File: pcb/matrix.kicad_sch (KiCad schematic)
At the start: 69 parts, among them J1 Conn_01x02, J2 USB_C_Receptacle_USB2.0_14P, SW1 SW_Push, SW2 SW_Push, SW3 SW_Push, SW4 SW_Push, U1 ESP32-S3-MINI-1U, U2 AP2112K-3.3

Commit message: Update silkscreen
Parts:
- renumbered TP9 to 3V3, TP8 to BAT1, TP1 to CP1, TP2 to CP2, TP3 to CP3, TP4 to CP4, TP5 to CP5, TP6 to CP6, TP7 to GND1, TP10 to USB1
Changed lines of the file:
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@@
 		(dnp no)
 		(fields_autoplaced yes)
-		(property "Reference" "TP1"
+		(property "Reference" "CP1"
 			(at 200.66 94.7419 0)
 			(effects
@@
 			(project ""
 				(path "/dedde073-c051-4814-9913-31ee2067ce3b"
-					(reference "TP1")
+					(reference "CP1")
 					(unit 1)
 				)
@@
 		(dnp no)
 		(fields_autoplaced yes)
-		(property "Reference" "TP10"
+		(property "Reference" "USB1"
 			(at 82.55 47.4979 0)
 			(effects
@@
 			(project ""
 				(path "/dedde073-c051-4814-9913-31ee2067ce3b"
-					(reference "TP10")
+					(reference "USB1")
 					(unit 1)
 				)
@@
 		(dnp no)
 		(fields_autoplaced yes)
-		(property "Reference" "TP6"
+		(property "Reference" "CP6"
 			(at 200.66 132.8419 0)
 			(effects
@@
 			(project "simple"
 				(path "/dedde073-c051-4814-9913-31ee2067ce3b"
-					(reference "TP6")
+					(reference "CP6")
 					(unit 1)
 				)
@@
 		(dnp no)
 		(fields_autoplaced yes)
-		(property "Reference" "TP7"
+		(property "Reference" "GND1"
 			(at 62.23 134.1119 0)
 			(effects
@@
 			(project ""
 				(path "/dedde073-c051-4814-9913-31ee2067ce3b"
-					(reference "TP7")
+					(reference "GND1")
 					(unit 1)
 				)
@@
 		(dnp no)
 		(fields_autoplaced yes)
-		(property "Reference" "TP9"
+		(property "Reference" "3V3"
 			(at 99.568 82.55 90)
 			(effects
@@
 			(project ""
 				(path "/dedde073-c051-4814-9913-31ee2067ce3b"
-					(reference "TP9")
+					(reference "3V3")
 					(unit 1)
 				)
@@
 		(dnp no)
 		(fields_autoplaced yes)
-		(property "Reference" "TP3"
+		(property "Reference" "CP3"
 			(at 200.66 109.9819 0)
 			(effects
@@
 			(project "simple"
 				(path "/dedde073-c051-4814-9913-31ee2067ce3b"
-					(reference "TP3")
+					(reference "CP3")
 					(unit 1)
 				)
@@
 		(dnp no)
 		(fields_autoplaced yes)
-		(property "Reference" "TP2"
+		(property "Reference" "CP2"
 			(at 200.66 102.3619 0)
 			(effects
@@
 			(project "simple"
 				(path "/dedde073-c051-4814-9913-31ee2067ce3b"
-					(reference "TP2")
+					(reference "CP2")
 					(unit 1)
 				)
@@
 		(dnp no)
 		(fields_autoplaced yes)
-		(property "Reference" "TP8"
+		(property "Reference" "BAT1"
 			(at 62.23 117.3479 0)
 			(effects
@@
 			(project ""
 				(path "/dedde073-c051-4814-9913-31ee2067ce3b"
-					(reference "TP8")
+					(reference "BAT1")
 					(unit 1)
 				)
@@
 		(dnp no)
 		(fields_autoplaced yes)
-		(property "Reference" "TP5"
+		(property "Reference" "CP5"
 			(at 200.66 125.2219 0)
 			(effects
@@
 			(project "simple"
 				(path "/dedde073-c051-4814-9913-31ee2067ce3b"
-					(reference "TP5")
+					(reference "CP5")
 					(unit 1)
 				)
@@
 		(dnp no)
 		(fields_autoplaced yes)
-		(property "Reference" "TP4"
+		(property "Reference" "CP4"
 			(at 200.66 117.6019 0)
 			(effects
@@
 			(project "simple"
 				(path "/dedde073-c051-4814-9913-31ee2067ce3b"
-					(reference "TP4")
+					(reference "CP4")
 					(unit 1)
 				)

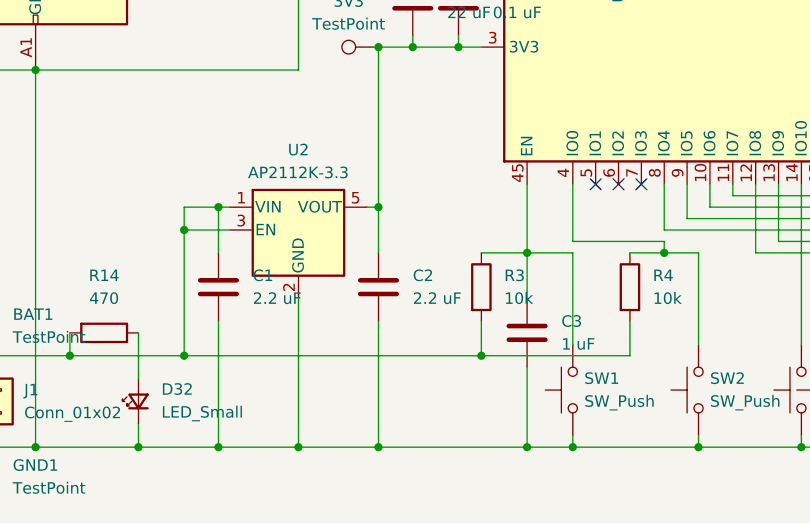
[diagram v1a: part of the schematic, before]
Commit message: Fix incorrect voltage
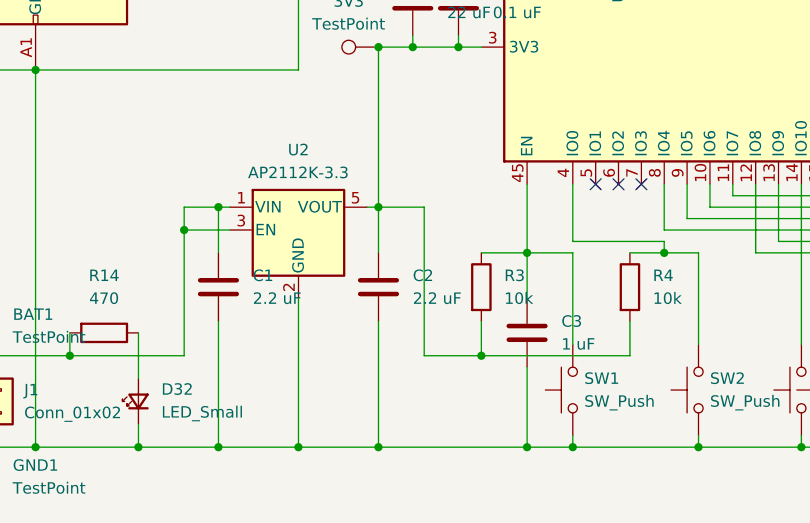
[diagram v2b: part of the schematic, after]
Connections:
- net at 3V3.1, C2.1, C4.2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: now also R3.2, R4.2
- net at BAT1.1, C1.1, J1.1 (Pin_1)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: no longer R3.2, R4.2
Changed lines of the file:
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@@
 	)
 	(junction
+		(at 114.3 121.92)
+		(diameter 0)
+		(color 0 0 0 0)
+	)
+	(junction
 		(at 55.88 125.73)
 		(diameter 0)
@@
 	)
 	(junction
-		(at 114.3 121.92)
-		(diameter 0)
-		(color 0 0 0 0)
-	)
-	(junction
 		(at 102.87 105.41)
 		(diameter 0)
@@
 	)
 	(junction
-		(at 81.28 121.92)
-		(diameter 0)
-		(color 0 0 0 0)
-	)
-	(junction
 		(at 204.47 121.92)
 		(diameter 0)
@@
 	(wire
 		(pts
-			(xy 81.28 121.92) (xy 114.3 121.92)
-		)
-		(stroke
-			(width 0)
-			(type default)
-		)
-	)
-	(wire
-		(pts
 			(xy 214.63 100.33) (xy 212.09 100.33)
 		)
@@
 	(wire
 		(pts
+			(xy 102.87 105.41) (xy 107.95 105.41)
+		)
+		(stroke
+			(width 0)
+			(type default)
+		)
+	)
+	(wire
+		(pts
 			(xy 240.03 114.3) (xy 242.57 114.3)
 		)
@@
 	(wire
 		(pts
-			(xy 130.81 118.11) (xy 130.81 121.92)
-		)
-		(stroke
-			(width 0)
-			(type default)
-		)
-	)
-	(wire
-		(pts
 			(xy 232.41 121.92) (xy 234.95 121.92)
 		)
@@
 	(wire
 		(pts
+			(xy 107.95 121.92) (xy 114.3 121.92)
+		)
+		(stroke
+			(width 0)
+			(type default)
+		)
+	)
+	(wire
+		(pts
 			(xy 214.63 107.95) (xy 214.63 106.68)
 		)
@@
 	(wire
 		(pts
-			(xy 114.3 121.92) (xy 130.81 121.92)
-		)
-		(stroke
-			(width 0)
-			(type default)
-		)
-	)
-	(wire
-		(pts
 			(xy 184.15 100.33) (xy 189.23 100.33)
 		)
@@
 	(wire
 		(pts
+			(xy 130.81 121.92) (xy 130.81 118.11)
+		)
+		(stroke
+			(width 0)
+			(type default)
+		)
+	)
+	(wire
+		(pts
 			(xy 229.87 101.6) (xy 232.41 101.6)
 		)
@@
 	(wire
 		(pts
+			(xy 114.3 121.92) (xy 130.81 121.92)
+		)
+		(stroke
+			(width 0)
+			(type default)
+		)
+	)
+	(wire
+		(pts
 			(xy 237.49 130.81) (xy 237.49 129.54)
 		)
@@
 		)
 		(stroke
+			(width 0)
+			(type default)
+		)
+	)
+	(wire
+		(pts
+			(xy 107.95 105.41) (xy 107.95 121.92)
+		)
+		(stroke

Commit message: Update parts
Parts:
- removed U2: AP2112K-3.3, Package_TO_SOT_SMD:SOT-23-5, symbol Regulator_Linear:AP2112K-3.3
- added U2: XC6206PxxxMR, Package_TO_SOT_SMD:SOT-23-3, symbol Regulator_Linear:XC6206PxxxMR
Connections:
- net GND: now also U2.1 (GND)
- net at 3V3.1, C2.1, C4.2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: now also U2.2 (VO)
- net at BAT1.1, C1.1, J1.1 (Pin_1)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: now also U2.3 (VI)
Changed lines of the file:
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@@
 	)
 	(junction
+		(at 93.98 132.08)
+		(diameter 0)
+		(color 0 0 0 0)
+	)
+	(junction
 		(at 227.33 99.06)
 		(diameter 0)
@@
 	)
 	(junction
-		(at 93.98 132.08)
-		(diameter 0)
-		(color 0 0 0 0)
-	)
-	(junction
 		(at 207.01 129.54)
 		(diameter 0)
@@
 	)
 	(junction
-		(at 81.28 107.95)
-		(diameter 0)
-		(color 0 0 0 0)
-	)
-	(junction
 		(at 207.01 93.98)
 		(diameter 0)
@@
 	(wire
 		(pts
-			(xy 93.98 115.57) (xy 93.98 132.08)
-		)
-		(stroke
-			(width 0)
-			(type default)
-		)
-	)
-	(wire
-		(pts
 			(xy 199.39 100.33) (xy 198.12 100.33)
 		)
@@
 	(wire
 		(pts
-			(xy 85.09 132.08) (xy 93.98 132.08)
+			(xy 93.98 113.03) (xy 93.98 132.08)
 		)
 		(stroke
@@
 	(wire
 		(pts
+			(xy 93.98 132.08) (xy 102.87 132.08)
+		)
+		(stroke
+			(width 0)
+			(type default)
+		)
+	)
+	(wire
+		(pts
 			(xy 111.76 63.5) (xy 179.07 63.5)
 		)
@@
 	(wire
 		(pts
-			(xy 81.28 105.41) (xy 81.28 107.95)
-		)
-		(stroke
-			(width 0)
-			(type default)
-		)
-	)
-	(wire
-		(pts
 			(xy 233.68 116.84) (xy 234.95 116.84)
 		)
@@
 	(wire
 		(pts
-			(xy 93.98 132.08) (xy 102.87 132.08)
+			(xy 85.09 132.08) (xy 93.98 132.08)
 		)
 		(stroke
@@
 	(wire
 		(pts
-			(xy 81.28 107.95) (xy 81.28 121.92)
+			(xy 81.28 105.41) (xy 81.28 121.92)
 		)
 		(stroke
@@
 	(wire
 		(pts
-			(xy 81.28 107.95) (xy 86.36 107.95)
-		)
-		(stroke
-			(width 0)
-			(type default)
-		)
-	)
-	(wire
-		(pts
 			(xy 210.82 127) (xy 210.82 124.46)
 		)
@@
 	)
 	(symbol
+		(lib_id "Regulator_Linear:XC6206PxxxMR")
+		(at 93.98 105.41 0)
+		(unit 1)
+		(exclude_from_sim no)
+		(in_bom yes)
+		(on_board yes)
+		(dnp no)
+		(fields_autoplaced yes)
+		(property "Reference" "U2"
+			(at 93.98 99.06 0)
+			(effects
+				(font
+					(size 1.27 1.27)
+				)
+			)
+		)
+		(property "Value" "XC6206PxxxMR"
+			(at 93.98 101.6 0)
+			(effects
+				(font
+					(size 1.27 1.27)
+				)
+			)
+		)
+		(property "Footprint" "Package_TO_SOT_SMD:SOT-23-3"
+			(at 93.98 99.695 0)
+			(effects
+				(font
+					(size 1.27 1.27)
+					(italic yes)
+				)
+				(hide yes)
+			)
+		)
+		(property "Datasheet" "https://www.torexsemi.com/file/xc6206/XC6206.pdf"
+			(at 93.98 105.41 0)
+			(effects
+				(font
+					(size 1.27 1.27)
+				)
+				(hide yes)
+			)
+		)
+		(property "Description" "Positive 60-250mA Low Dropout Regulator, Fixed Output, SOT-23"
+			(at 93.98 105.41 0)
+			(effects
+				(font
+					(size 1.27 1.27)
+				)
+				(hide yes)
+			)
+		)
+		(pin "3"
+		)
+		(pin "1"
+		)
+		(pin "2"
+		)
+		(instances
+			(project ""
+				(path "/dedde073-c051-4814-9913-31ee2067ce3b"
+					(reference "U2")
+					(unit 1)
+				)
+			)
+		)
+	)
+	(symbol
 		(lib_id "Device:C")
 		(at 102.87 114.3 0)
@@
 					(unit 1)
 				)
-			)
-		)
-	)
-	(symbol
-		(lib_id "Regulator_Linear:AP2112K-3.3")
-		(at 93.98 107.95 0)
-		(unit 1)
-		(exclude_from_sim no)
-		(in_bom yes)
-		(on_board yes)
-		(dnp no)
-		(fields_autoplaced yes)
-		(property "Reference" "U2"
-			(at 93.98 99.06 0)
-			(effects
-				(font
-					(size 1.27 1.27)
-				)
-			)
-		)
-		(property "Value" "AP2112K-3.3"
-			(at 93.98 101.6 0)
-			(effects
-				(font
-					(size 1.27 1.27)
-				)
-			)
-		)
-		(property "Footprint" "Package_TO_SOT_SMD:SOT-23-5"
-			(at 93.98 99.695 0)
-			(effects
-				(font
-					(size 1.27 1.27)
-				)
-				(hide yes)
-			)
-		)
-		(property "Datasheet" "https://www.diodes.com/assets/Datasheets/AP2112.pdf"
-			(at 93.98 105.41 0)
-			(effects
-				(font
-					(size 1.27 1.27)
-				)
-				(hide yes)
-			)
-		)
-		(property "Description" "600mA low dropout linear regulator, with enable pin, 3.8V-6V input voltage range, 3.3V fixed positive output, SOT-23-5"
-			(at 93.98 107.95 0)
-			(effects
-				(font
-					(size 1.27 1.27)
-				)
-				(hide yes)
-			)
-		)
-		(pin "3"
-		)
-		(pin "1"
-		)
-		(pin "4"
-		)
-		(pin "2"
-		)
-		(pin "5"
-		)
-		(instances
-			(project "simple"
-				(path "/dedde073-c051-4814-9913-31ee2067ce3b"
-					(reference "U2")
-					(unit 1)
-				)

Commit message: Replace components
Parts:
- removed SW4: SW_Push, Button_Switch_SMD:SW_SPST_PTS810, symbol Switch:SW_Push
- removed U1: ESP32-S3-MINI-1U, RF_Module:ESP32-S2-MINI-1U, symbol RF_Module:ESP32-S3-MINI-1U
- added U1: ESP32-C3-WROOM-02, RF_Module:ESP32-C3-WROOM-02, symbol RF_Module:ESP32-C3-WROOM-02
- SW1, SW2, SW3: footprint Button_Switch_SMD:SW_SPST_PTS810 -> Button_Switch_SMD:SW_SPST_TS-1088-xR020
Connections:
- net GND: now also U1.19 (GND), U1.9 (GND)
- net at 3V3.1, C2.1, C4.2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: now also U1.1 (3V3)
- net P5: now reaches R9.1
- net P5: now also U1.15 (IO3)
- net P4: now reaches R8.1
- net P4: now also U1.3 (IO4)
- net P3: now reaches R7.1
- net P3: now also U1.4 (IO5)
- net P2: now reaches R6.1
- net P2: now also U1.5 (IO6)
- net P1: now reaches R5.1
- net P1: now also U1.6 (IO7)
- net at SW3.2: now also U1.10 (IO10)
- net USB-: now reaches R11.2
- net USB-: now also U1.13 (IO18)
- net USB+: now reaches R12.2
- net USB+: now also U1.14 (IO19)
- net at R4.1, SW2.2: now also U1.18 (IO0)
- net at C3.1, R3.1, SW1.2: now also U1.2 (EN)
- net P6: now reaches R10.1
- net P6: now also U1.17 (IO1)
- no-connect marks 26 -> 5
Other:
- moved on the sheet: CP1, CP2, CP3, CP4, CP5, CP6, D1, D10, D11, D12, D13, D14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

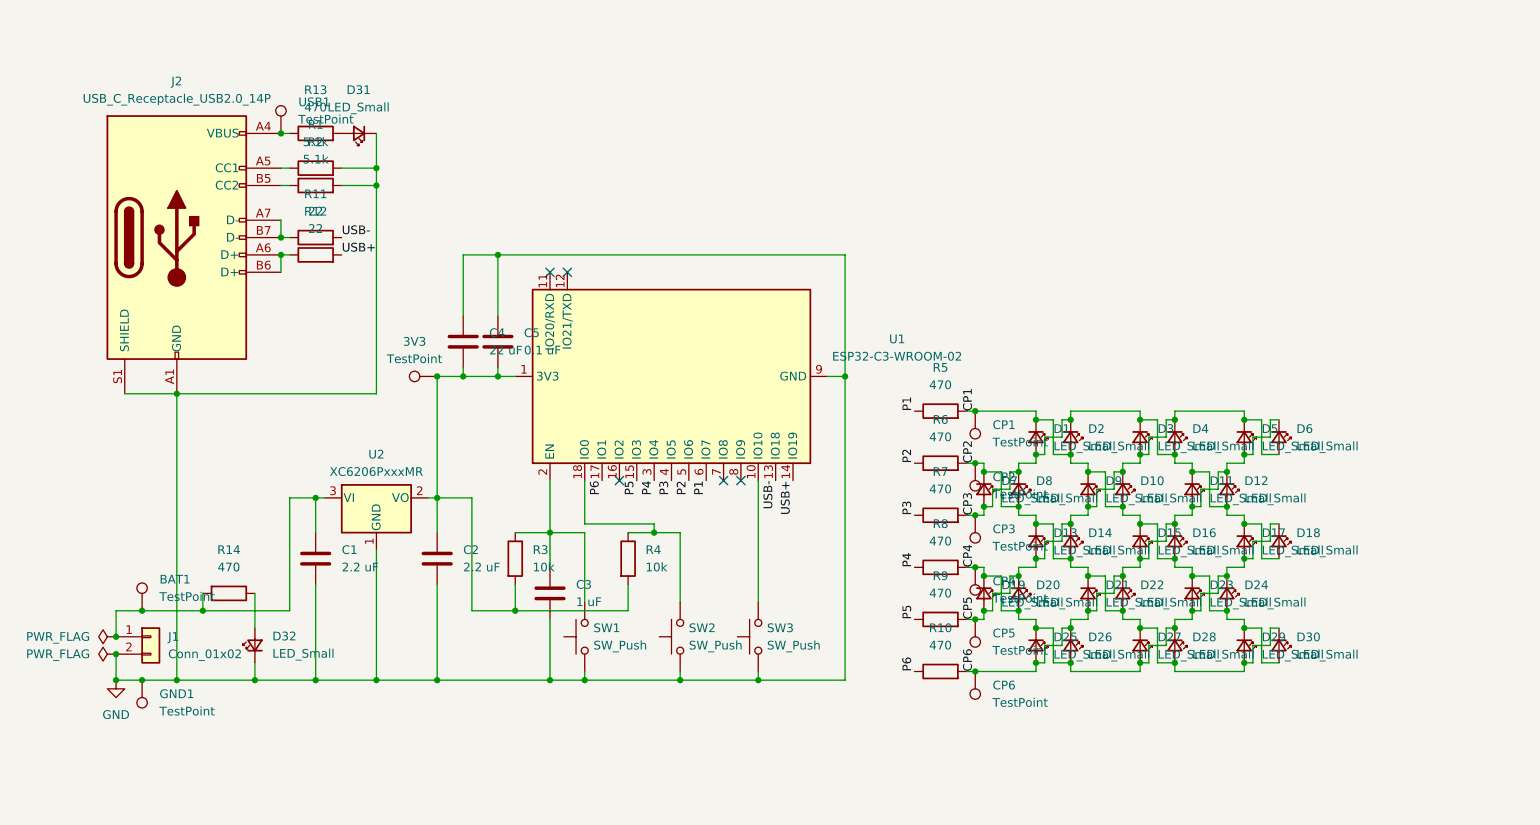
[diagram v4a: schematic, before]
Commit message: Update to C6-MINI
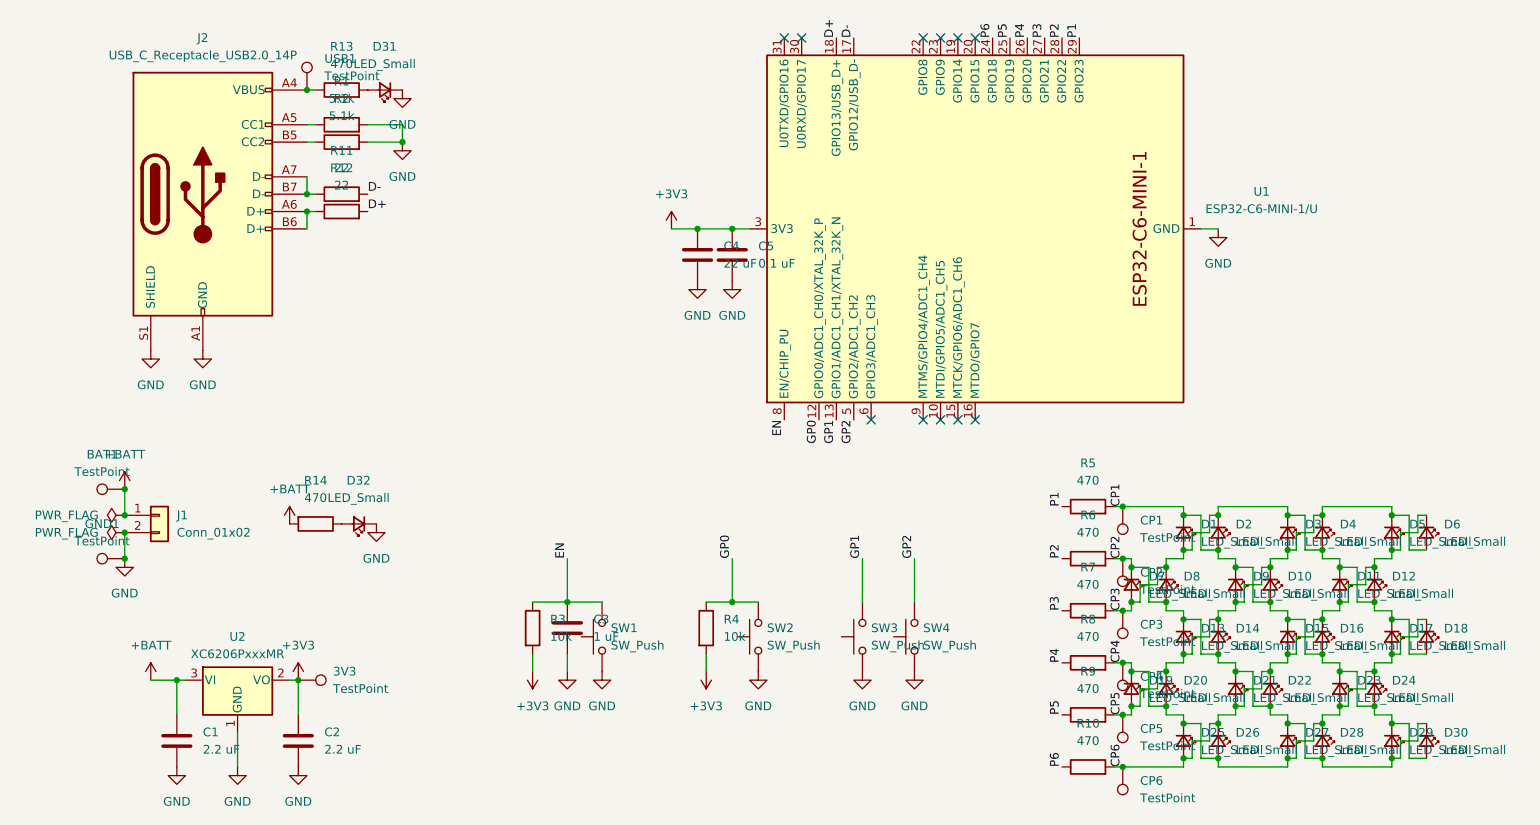
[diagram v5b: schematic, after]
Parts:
- removed U1: ESP32-C3-WROOM-02, RF_Module:ESP32-C3-WROOM-02, symbol RF_Module:ESP32-C3-WROOM-02
- added SW4: SW_Push, Button_Switch_SMD:SW_SPST_TS-1088-xR020, symbol Switch:SW_Push
- added U1: ESP32-C6-MINI-1/U, PCM_Espressif:ESP32-C6-MINI-1U, symbol PCM_Espressif:ESP32-C6-MINI-1/U
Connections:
- net GND: now also C4.2, C5.2, SW4.1, U1.1 (GND), U1.11 (GND), U1.14 (GND), U1.2 (GND), U1.36 (GND), U1.37 (GND), U1.38 (GND), U1.39 (GND), U1.40 (GND), U1.41 (GND), U1.42 (GND), U1.43 (GND), U1.44 (GND), U1.45 (GND), U1.46 (GND), U1.47 (GND), U1.48 (GND), U1.49 (GND), U1.50 (GND), U1.51 (GND), U1.52 (GND), U1.53 (GND); no longer C4.1, C5.1
- net P1: now also U1.29 (GPIO23)
- net P2: now also U1.28 (GPIO22)
- net P3: now also U1.27 (GPIO21)
- net P4: now also U1.26 (GPIO20)
- net P5: now also U1.25 (GPIO19)
- net P6: now also U1.24 (GPIO18)
- net +3V3: now reaches 3V3.1, C2.1, R3.2, R4.2, U2.2 (VO)
- net +3V3: now also C4.1, C5.1, U1.3 (3V3); no longer C4.2, C5.2
- net +BATT: now reaches BAT1.1, C1.1, J1.1 (Pin_1), R14.2, U2.3 (VI)
- net GP0: now reaches R4.1, SW2.2
- net GP0: now also U1.12 (GPIO0/ADC1_CH0/XTAL_32K_P)
- net EN: now reaches C3.1, R3.1, SW1.2
- net EN: now also U1.8 (EN/CHIP_PU)
- net GP1: now reaches SW3.2
- net GP1: now also U1.13 (GPIO1/ADC1_CH1/XTAL_32K_N)
- net USB+ renamed D+
- net D+: now also U1.18 (GPIO13/USB_D+)
- net USB- renamed D-
- net D-: now also U1.17 (GPIO12/USB_D-)
- new net GP2: SW4.2, U1.5 (GPIO2/ADC1_CH2)
- no-connect marks 5 -> 11
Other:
- moved on the sheet: 3V3, BAT1, C1, C2, C3, C4, C5, CP1, CP2, CP3, CP4, CP5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
